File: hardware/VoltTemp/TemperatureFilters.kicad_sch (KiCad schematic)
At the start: 0 parts

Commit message: schematic mostly done
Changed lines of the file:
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@@
 	)
 	(bus_entry
-		(at 78.74 67.31)
+		(at 78.74 68.58)
 		(size 2.54 -2.54)
 		(stroke
@@
 		)
 	)
+	(wire
+		(pts
+			(xy 81.28 66.04) (xy 99.06 66.04)
+		)
+		(stroke
+			(width 0)
+			(type default)
+		)
+	)
 	(bus
 		(pts
@@
 	(wire
 		(pts
-			(xy 81.28 64.77) (xy 99.06 64.77)
-		)
-		(stroke
-			(width 0)
-			(type default)
-		)
-	)
-	(wire
-		(pts
 			(xy 81.28 81.28) (xy 99.06 81.28)
 		)
@@
 	(bus
 		(pts
-			(xy 78.74 67.31) (xy 78.74 83.82)
+			(xy 78.74 68.58) (xy 78.74 83.82)
 		)
 		(stroke
@@
 	(bus
 		(pts
-			(xy 78.74 63.5) (xy 78.74 67.31)
-		)
-		(stroke
-			(width 0)
-			(type default)
-		)
-	)
-	(label "Temperature1"
+			(xy 78.74 63.5) (xy 78.74 68.58)
+		)
+		(stroke
+			(width 0)
+			(type default)
+		)
+	)
+	(label "Temperature0"
 		(at 132.08 66.04 0)
 		(effects
@@
 		)
 	)
-	(label "Temperature2"
+	(label "Temperature1"
 		(at 132.08 81.28 0)
 		(effects
@@
 	)
 	(label "rawTemperature0"
-		(at 81.28 64.77 0)
+		(at 81.28 66.04 0)
 		(effects
 			(font
@@
 		)
 		(pin "tempIn" input
-			(at 99.06 64.77 180)
-			(effects
-				(font
+			(at 99.06 66.04 180)
+			(effects
+				(font

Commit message: layout
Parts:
- added TP10, TP6, TP7, TP8, TP9: TP_TempIn, TestPoint:TestPoint_Pad_1.0x1.0mm, symbol Connector:TestPoint
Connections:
- net rawTemperature0: now also TP6.1
- net rawTemperature1: now also TP7.1
- net rawTemperature2: now also TP8.1
- net rawTemperature3: now also TP9.1
- net rawTemperature4: now also TP10.1

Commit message: layout2 electric boogaloo
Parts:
- TP6: footprint TestPoint:TestPoint_Pad_1.0x1.0mm -> TestPoint:TestPoint_Pad_D1.0mm
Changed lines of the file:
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@@
 			)
 		)
-		(property "Footprint" "TestPoint:TestPoint_Pad_1.0x1.0mm"
+		(property "Footprint" "TestPoint:TestPoint_Pad_D1.0mm"
 			(at 80.01 66.04 0)
 			(effects

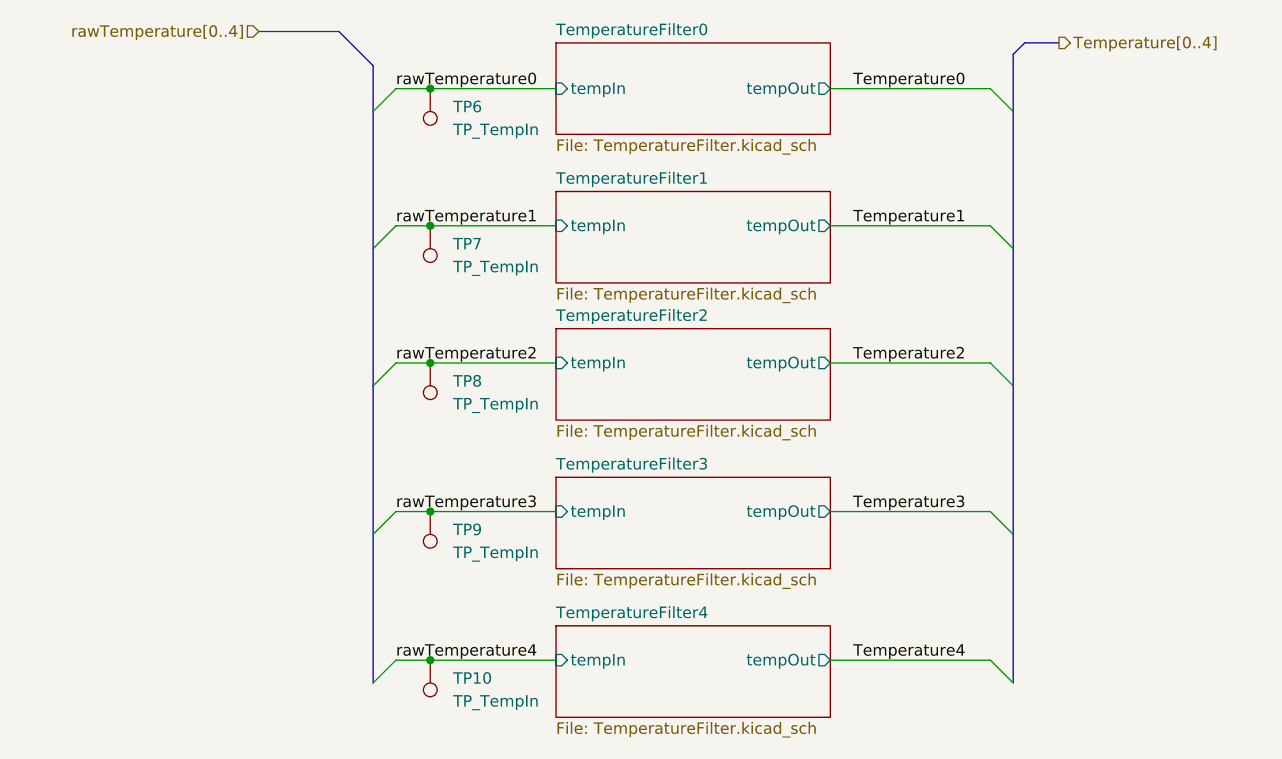
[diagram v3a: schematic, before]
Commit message: add thermistor test board, just need to route volttemp testpoints
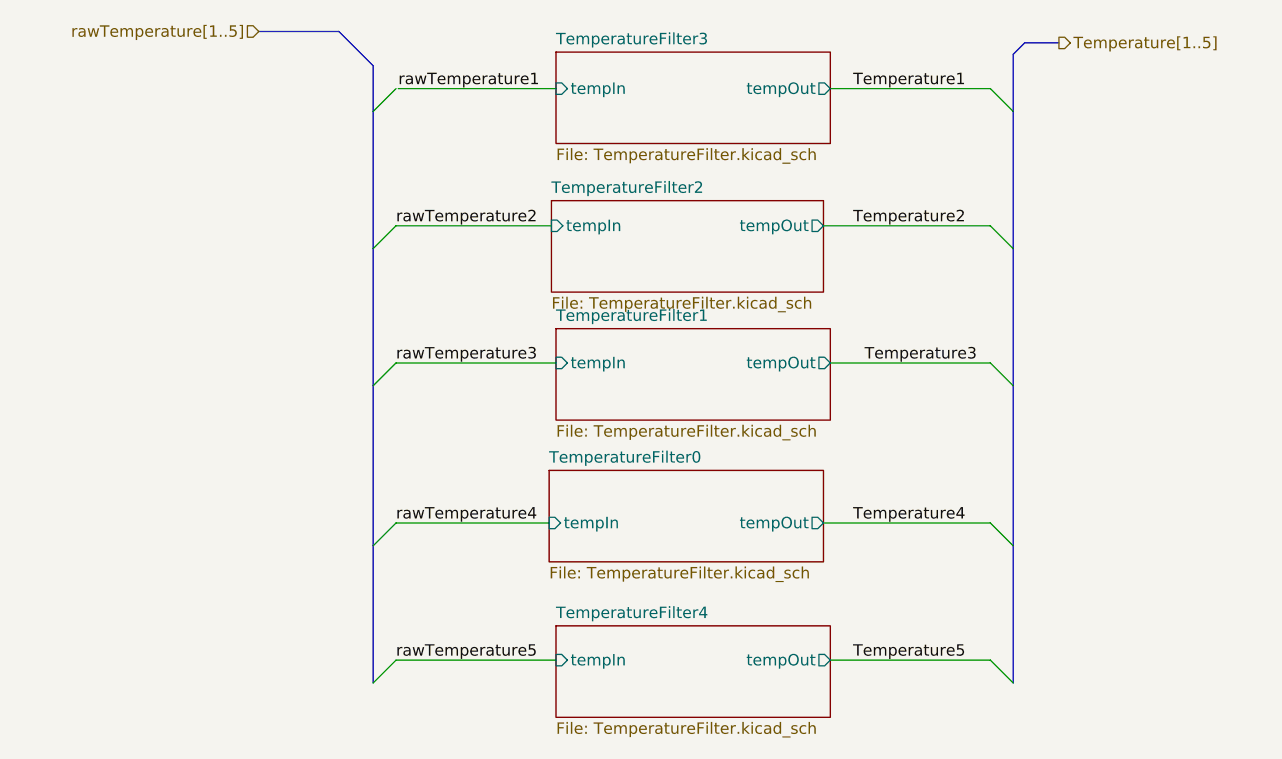
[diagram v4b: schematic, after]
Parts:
- removed TP10, TP7, TP8, TP9: TP_TempIn, TestPoint:TestPoint_Pad_1.0x1.0mm, symbol Connector:TestPoint
- removed TP6: TP_TempIn, TestPoint:TestPoint_Pad_D1.0mm, symbol Connector:TestPoint
